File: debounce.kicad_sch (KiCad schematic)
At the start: 4 parts, among them J2 Conn_02x10_Odd_Even, U5 4070, U6 4013, U7 4017

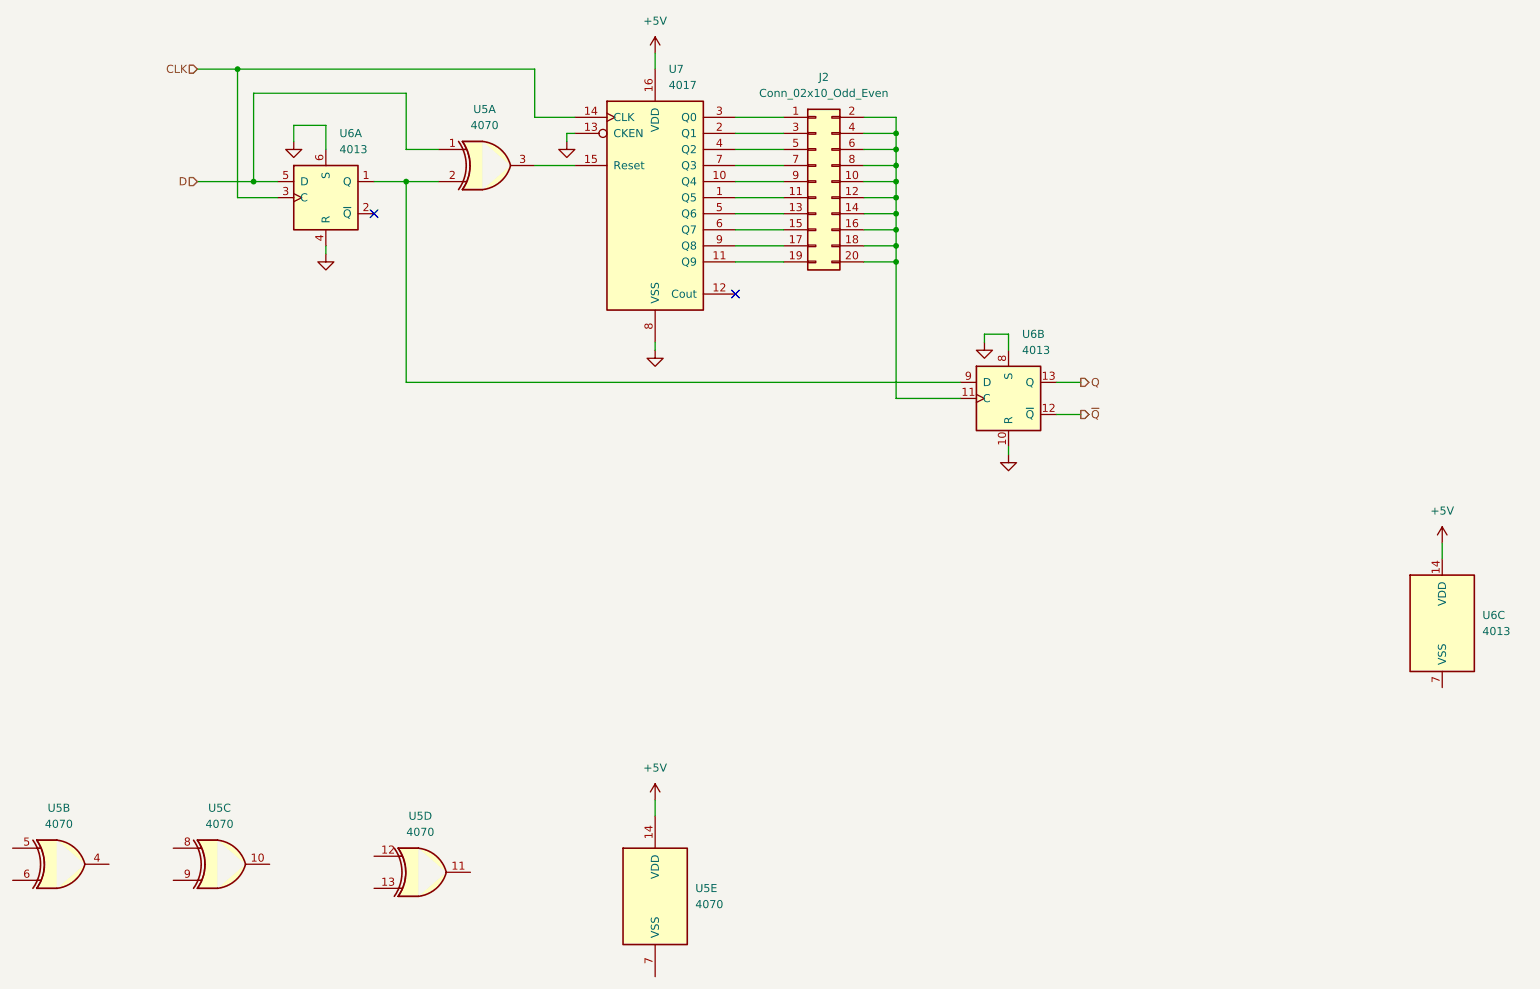
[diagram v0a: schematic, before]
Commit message: More hierarchical; adding debounce
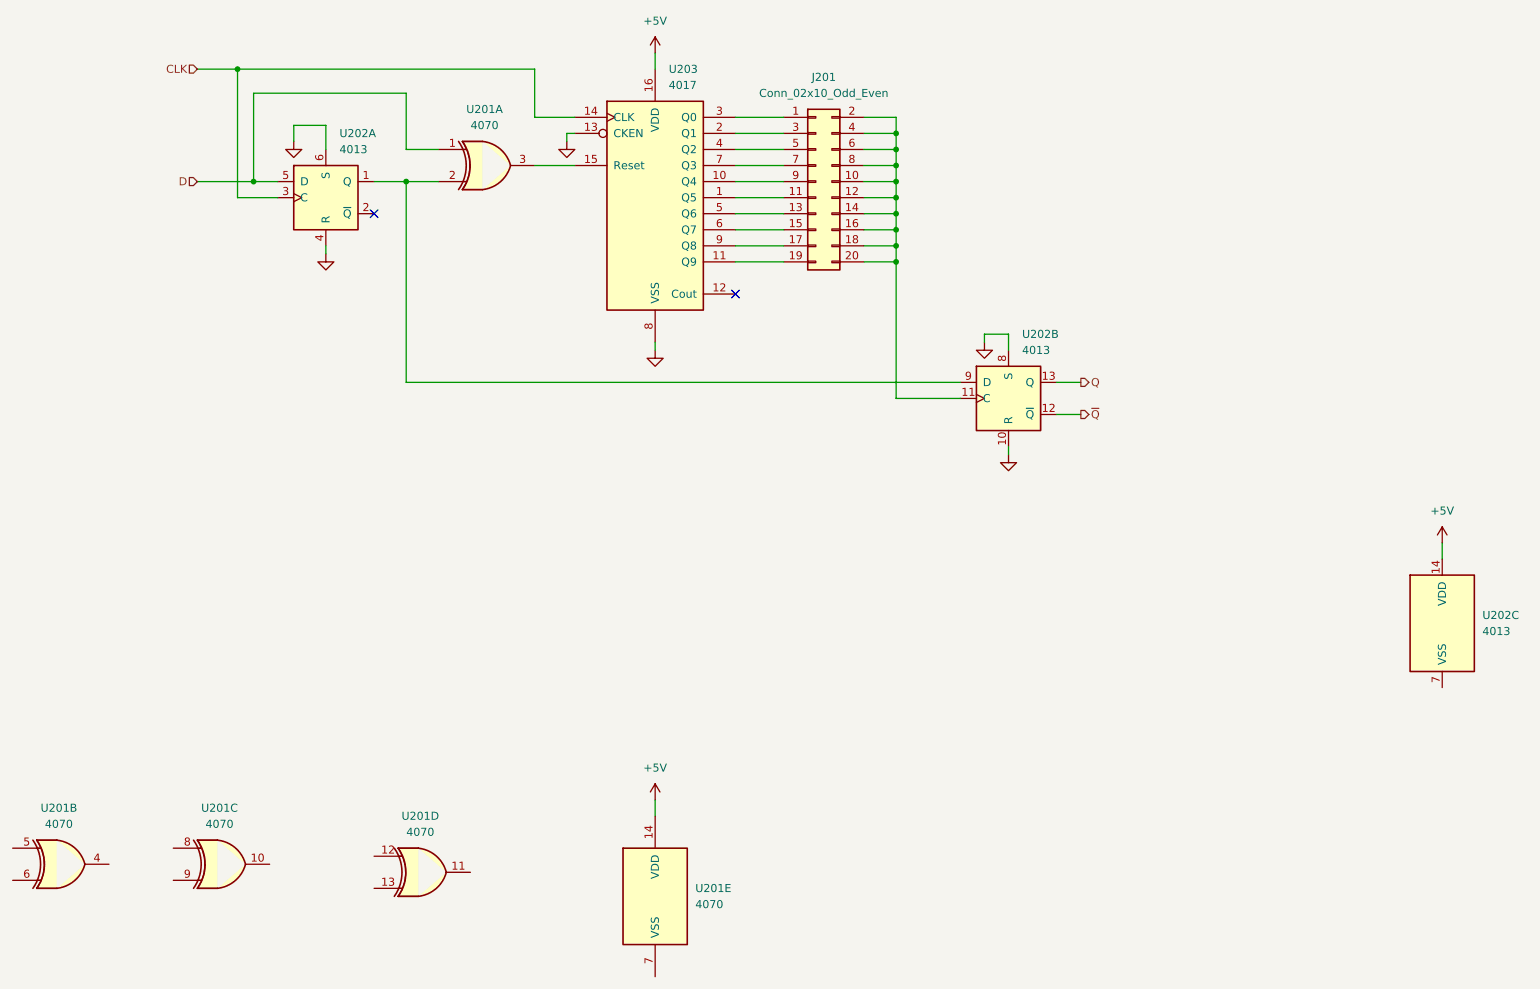
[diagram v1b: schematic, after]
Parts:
- renumbered J2 to J201, U5 to U201, U6 to U202, U7 to U203
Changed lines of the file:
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@@
 		(dnp no)
 		(fields_autoplaced yes)
-		(property "Reference" "U6"
+		(property "Reference" "U202"
 			(at 264.16 130.8099 0)
 			(effects
@@
 			(project ""
 				(path "/8304b3b7-1ae3-4935-a8ef-a9ab1b0a3004/d52e23db-71ba-49ec-b03b-ab9ecdc3741b"
-					(reference "U6")
+					(reference "U202")
 					(unit 3)
 				)
@@
 		(dnp no)
 		(fields_autoplaced yes)
-		(property "Reference" "U7"
+		(property "Reference" "U203"
 			(at 135.4933 44.45 0)
 			(effects
@@
 			(project ""
 				(path "/8304b3b7-1ae3-4935-a8ef-a9ab1b0a3004/d52e23db-71ba-49ec-b03b-ab9ecdc3741b"
-					(reference "U7")
+					(reference "U203")
 					(unit 1)
 				)
@@
 		(dnp no)
 		(fields_autoplaced yes)
-		(property "Reference" "#PWR037"
+		(property "Reference" "#PWR0204"
 			(at 81.28 80.01 0)
 			(effects
@@
 			(project "garagelights"
 				(path "/8304b3b7-1ae3-4935-a8ef-a9ab1b0a3004/d52e23db-71ba-49ec-b03b-ab9ecdc3741b"
-					(reference "#PWR037")
+					(reference "#PWR0204")
 					(unit 1)
 				)
@@
 		(dnp no)
 		(fields_autoplaced yes)
-		(property "Reference" "#PWR036"
+		(property "Reference" "#PWR0206"
 			(at 133.35 95.25 0)
 			(effects
@@
 			(project ""
 				(path "/8304b3b7-1ae3-4935-a8ef-a9ab1b0a3004/d52e23db-71ba-49ec-b03b-ab9ecdc3741b"
-					(reference "#PWR036")
+					(reference "#PWR0206")
 					(unit 1)
 				)
@@
 		(dnp no)
 		(fields_autoplaced yes)
-		(property "Reference" "#PWR042"
+		(property "Reference" "#PWR0201"
 			(at 133.35 45.72 0)
 			(effects
@@
 			(project ""
 				(path "/8304b3b7-1ae3-4935-a8ef-a9ab1b0a3004/d52e23db-71ba-49ec-b03b-ab9ecdc3741b"
-					(reference "#PWR042")
+					(reference "#PWR0201")
 					(unit 1)
 				)
@@
 		(dnp no)
 		(fields_autoplaced yes)
-		(property "Reference" "U5"
+		(property "Reference" "U201"
 			(at 139.7 173.9899 0)
 			(effects
@@
 			(project ""
 				(path "/8304b3b7-1ae3-4935-a8ef-a9ab1b0a3004/d52e23db-71ba-49ec-b03b-ab9ecdc3741b"
-					(reference "U5")
+					(reference "U201")
 					(unit 5)
 				)
@@
 		(dnp no)
 		(fields_autoplaced yes)
-		(property "Reference" "U6"
+		(property "Reference" "U202"
 			(at 191.3733 86.36 0)
 			(effects
@@
 			(project ""
 				(path "/8304b3b7-1ae3-4935-a8ef-a9ab1b0a3004/d52e23db-71ba-49ec-b03b-ab9ecdc3741b"
-					(reference "U6")
+					(reference "U202")
 					(unit 2)
 				)
@@
 		(dnp no)
 		(fields_autoplaced yes)
-		(property "Reference" "U5"
+		(property "Reference" "U201"
 			(at 106.3752 50.8 0)
 			(effects
@@
 			(project ""
 				(path "/8304b3b7-1ae3-4935-a8ef-a9ab1b0a3004/d52e23db-71ba-49ec-b03b-ab9ecdc3741b"
-					(reference "U5")
+					(reference "U201")
 					(unit 1)
 				)
@@
 		(dnp no)
 		(fields_autoplaced yes)
-		(property "Reference" "J2"
+		(property "Reference" "J201"
 			(at 160.02 45.72 0)
 			(effects
@@
 			(project ""
 				(path "/8304b3b7-1ae3-4935-a8ef-a9ab1b0a3004/d52e23db-71ba-49ec-b03b-ab9ecdc3741b"
-					(reference "J2")
+					(reference "J201")
 					(unit 1)
 				)
@@
 		(dnp no)
 		(fields_autoplaced yes)
-		(property "Reference" "#PWR039"
+		(property "Reference" "#PWR0203"
 			(at 119.38 62.23 0)
 			(effects
@@
 			(project "garagelights"
 				(path "/8304b3b7-1ae3-4935-a8ef-a9ab1b0a3004/d52e23db-71ba-49ec-b03b-ab9ecdc3741b"
-					(reference "#PWR039")
+					(reference "#PWR0203")
 					(unit 1)
 				)
@@
 		(dnp no)
 		(fields_autoplaced yes)
-		(property "Reference" "U5"
+		(property "Reference" "U201"
 			(at 96.2152 162.56 0)
 			(effects
@@
 			(project ""
 				(path "/8304b3b7-1ae3-4935-a8ef-a9ab1b0a3004/d52e23db-71ba-49ec-b03b-ab9ecdc3741b"
-					(reference "U5")
+					(reference "U201")
 					(unit 4)
 				)
@@
 		(dnp no)
 		(fields_autoplaced yes)
-		(property "Reference" "#PWR041"
+		(property "Reference" "#PWR0205"
 			(at 185.42 93.98 0)
 			(effects
@@
 			(project "garagelights"
 				(path "/8304b3b7-1ae3-4935-a8ef-a9ab1b0a3004/d52e23db-71ba-49ec-b03b-ab9ecdc3741b"
-					(reference "#PWR041")
+					(reference "#PWR0205")
 					(unit 1)
 				)
@@
 		(dnp no)
 		(fields_autoplaced yes)
-		(property "Reference" "#PWR044"
+		(property "Reference" "#PWR0209"
 			(at 133.35 163.83 0)
 			(effects
@@
 			(project ""
 				(path "/8304b3b7-1ae3-4935-a8ef-a9ab1b0a3004/d52e23db-71ba-49ec-b03b-ab9ecdc3741b"
-					(reference "#PWR044")
+					(reference "#PWR0209")
 					(unit 1)
 				)
@@
 		(dnp no)
 		(fields_autoplaced yes)
-		(property "Reference" "#PWR038"
+		(property "Reference" "#PWR0202"
 			(at 76.2 62.23 0)
 			(effects
@@
 			(project "garagelights"
 				(path "/8304b3b7-1ae3-4935-a8ef-a9ab1b0a3004/d52e23db-71ba-49ec-b03b-ab9ecdc3741b"
-					(reference "#PWR038")
+					(reference "#PWR0202")
 					(unit 1)
 				)
@@
 		(dnp no)
 		(fields_autoplaced yes)
-		(property "Reference" "U5"
+		(property "Reference" "U201"
 			(at 39.0652 161.29 0)
 			(effects
@@
 			(project ""
 				(path "/8304b3b7-1ae3-4935-a8ef-a9ab1b0a3004/d52e23db-71ba-49ec-b03b-ab9ecdc3741b"
-					(reference "U5")
+					(reference "U201")
 					(unit 2)
 				)
@@
 		(dnp no)
 		(fields_autoplaced yes)
-		(property "Reference" "U6"
+		(property "Reference" "U202"
 			(at 83.4233 54.61 0)
 			(effects
@@
 			(project ""
 				(path "/8304b3b7-1ae3-4935-a8ef-a9ab1b0a3004/d52e23db-71ba-49ec-b03b-ab9ecdc3741b"
-					(reference "U6")
+					(reference "U202")
 					(unit 1)
 				)
@@
 		(dnp no)
 		(fields_autoplaced yes)
-		(property "Reference" "#PWR043"
+		(property "Reference" "#PWR0208"
 			(at 257.81 123.19 0)
 			(effects
@@
 			(project ""
 				(path "/8304b3b7-1ae3-4935-a8ef-a9ab1b0a3004/d52e23db-71ba-49ec-b03b-ab9ecdc3741b"
-					(reference "#PWR043")
+					(reference "#PWR0208")
 					(unit 1)
 				)
@@
 		(dnp no)
 		(fields_autoplaced yes)
-		(property "Reference" "U5"
+		(property "Reference" "U201"
 			(at 64.4652 161.29 0)
 			(effects
@@
 			(project ""
 				(path "/8304b3b7-1ae3-4935-a8ef-a9ab1b0a3004/d52e23db-71ba-49ec-b03b-ab9ecdc3741b"
-					(reference "U5")
+					(reference "U201")
 					(unit 3)
 				)
@@
 		(dnp no)
 		(fields_autoplaced yes)
-		(property "Reference" "#PWR040"
+		(property "Reference" "#PWR0207"
 			(at 189.23 111.76 0)
 			(effects
@@
 			(project "garagelights"
 				(path "/8304b3b7-1ae3-4935-a8ef-a9ab1b0a3004/d52e23db-71ba-49ec-b03b-ab9ecdc3741b"
-					(reference "#PWR040")
+					(reference "#PWR0207")
 					(unit 1)
 				)
